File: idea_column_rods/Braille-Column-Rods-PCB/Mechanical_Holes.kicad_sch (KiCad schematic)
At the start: 14 parts

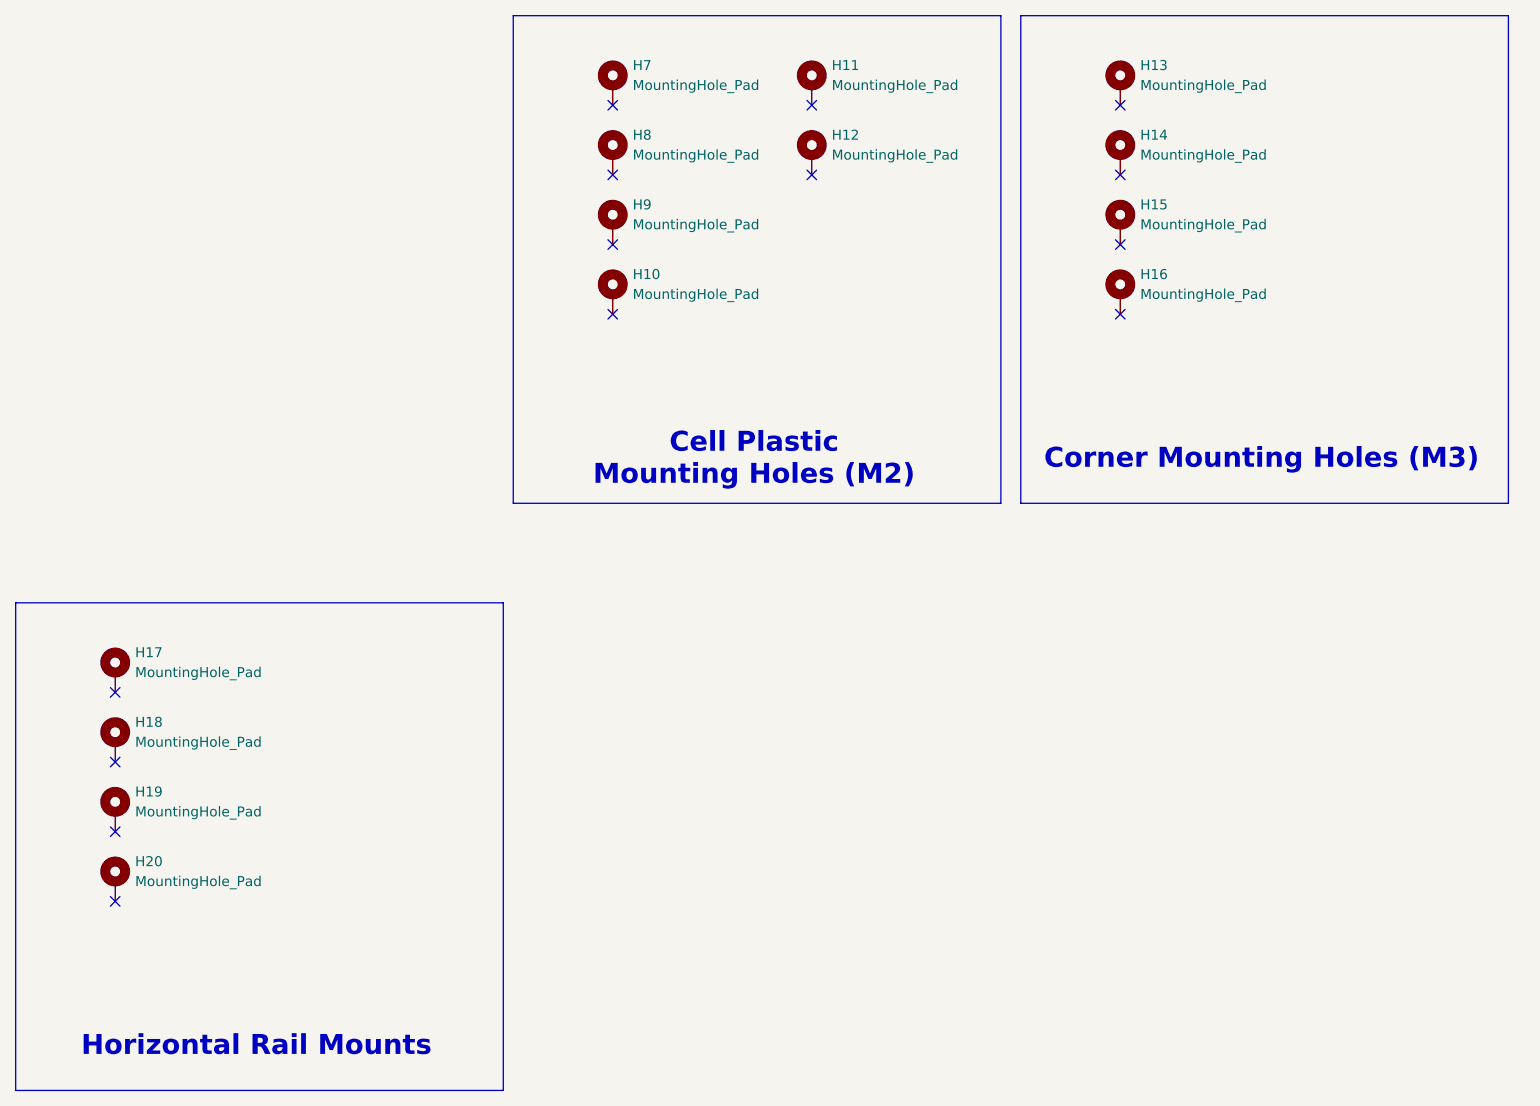
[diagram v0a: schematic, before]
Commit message: WIP: Rods PCB placement
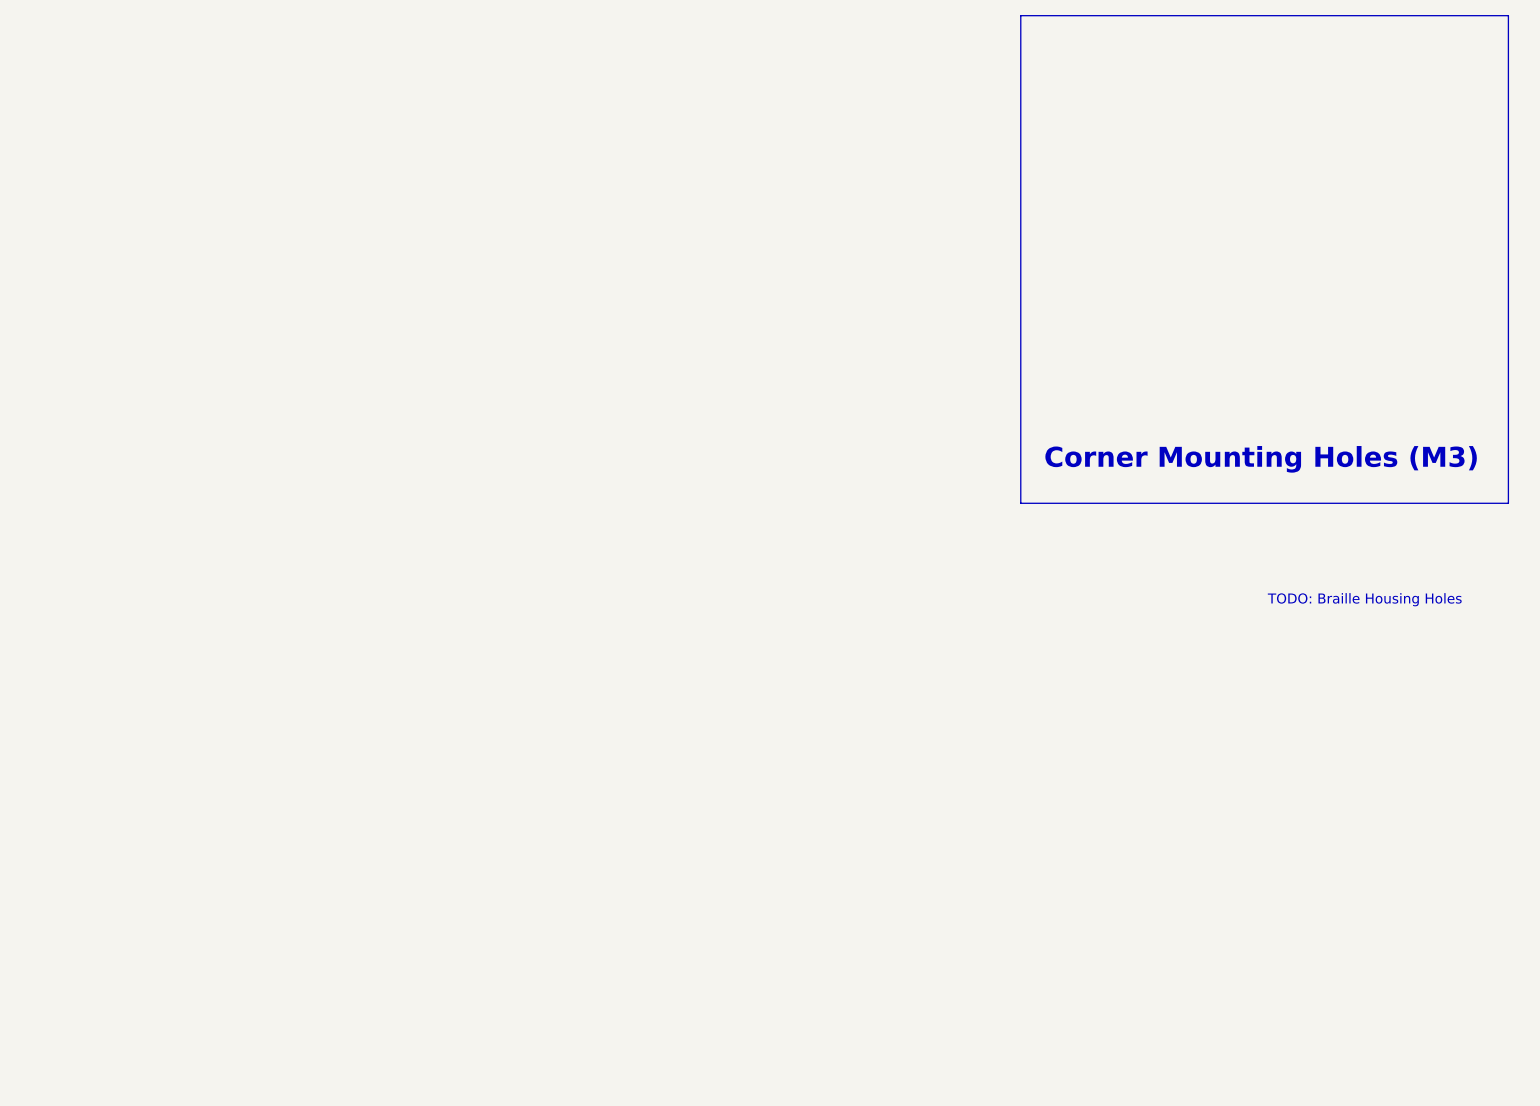
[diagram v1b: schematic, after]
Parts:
- removed H10, H11, H12, H7, H8, H9: MountingHole_Pad, 00-lib-footprints:MountingHole_2.2mm_M2_Pad_NoSilk, symbol Mechanical:MountingHole_Pad
- removed H13, H14, H15, H16: MountingHole_Pad, 00-lib-footprints:MountingHole_3.2mm_M3_Pad_NoSilk, symbol Mechanical:MountingHole_Pad
- removed H17, H18, H19, H20: MountingHole_Pad, 00-lib-footprints:HorizMounting_4x_M2_and_M3_Middle, symbol Mechanical:MountingHole_Pad
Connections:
- no-connect marks 14 -> 0
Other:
- note added: "TODO: Braille Housing Holes"
- note removed: "Cell Plastic Mounting Holes (M2)"
- note removed: "Horizontal Rail Mounts"

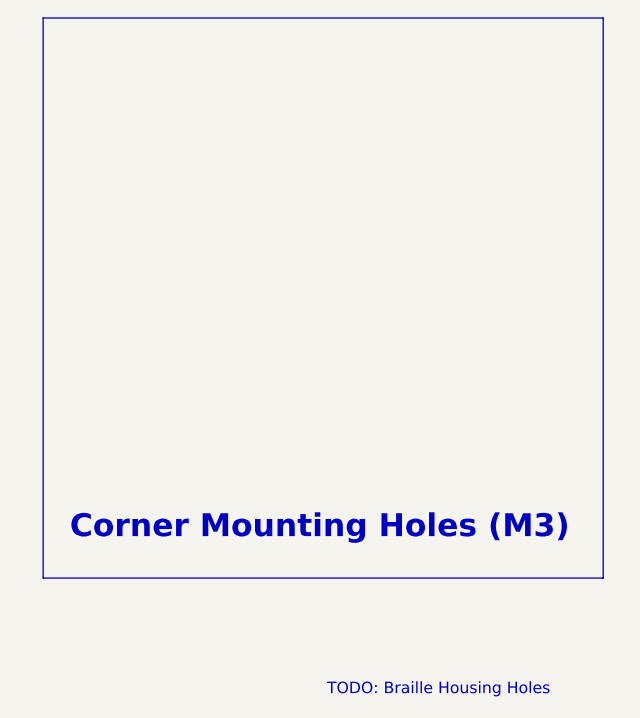
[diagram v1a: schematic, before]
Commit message: WIP: Place the housing and motor X
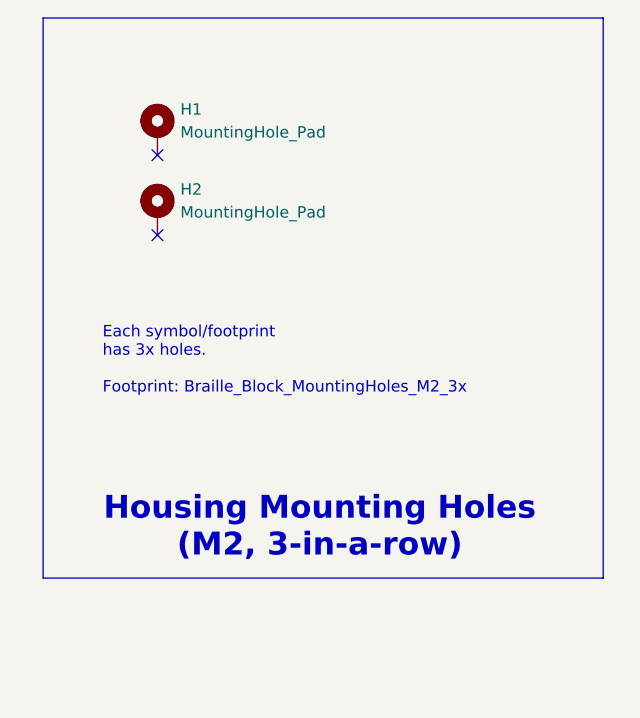
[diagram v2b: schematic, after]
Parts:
- added H1, H2: MountingHole_Pad, 00-lib-footprints:Braille_Block_MountingHoles_M2_3x, symbol Mechanical:MountingHole_Pad
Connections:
- no-connect marks 0 -> 2
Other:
- note added: "Each symbol/footprint has 3x holes. Footprint: Braille_Block_MountingHoles_M2_3x"
- note added: "Housing Mounting Holes (M2, 3-in-a-row)"
- note removed: "Corner Mounting Holes (M3)"
- note removed: "TODO: Braille Housing Holes"
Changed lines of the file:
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@@
 	(generator_version "8.0")
 	(paper "USLetter")
+	(no_connect
+		(at 168.91 50.8)
+	)
+	(no_connect
+		(at 168.91 41.91)
+	)
 	(rectangle
 		(start 156.21 26.67)
@@
 		)
 	)
-	(text "Corner Mounting Holes (M3)"
+	(text "Each symbol/footprint\nhas 3x holes.\n\nFootprint: Braille_Block_MountingHoles_M2_3x"
+		(exclude_from_sim no)
+		(at 162.814 64.77 0)
+		(effects
+			(font
+				(size 1.27 1.27)
+			)
+			(justify left)
+		)
+	)
+	(text "Housing Mounting Holes\n(M2, 3-in-a-row)"
 		(exclude_from_sim no)
 		(at 186.944 83.312 0)
@@
 		)
 	)
-	(text "TODO: Braille Housing Holes"
-		(exclude_from_sim no)
-		(at 200.152 101.346 0)
-		(effects
-			(font
-				(size 1.27 1.27)
+	(symbol
+		(lib_id "Mechanical:MountingHole_Pad")
+		(at 168.91 39.37 0)
+		(unit 1)
+		(exclude_from_sim yes)
+		(in_bom no)
+		(on_board yes)
+		(dnp no)
+		(fields_autoplaced yes)
+		(property "Reference" "H1"
+			(at 171.45 36.8299 0)
+			(effects
+				(font
+					(size 1.27 1.27)
+				)
+				(justify left)
 			)
 		)
+		(property "Value" "MountingHole_Pad"
+			(at 171.45 39.3699 0)
+			(effects
+				(font
+					(size 1.27 1.27)
+				)
+				(justify left)
+			)
+		)
+		(property "Footprint" "00-lib-footprints:Braille_Block_MountingHoles_M2_3x"
+			(at 168.91 39.37 0)
+			(effects
+				(font
+					(size 1.27 1.27)
+				)
+				(hide yes)
+			)
+		)
+		(property "Datasheet" "~"
+			(at 168.91 39.37 0)
+			(effects
+				(font
+					(size 1.27 1.27)
+				)
+				(hide yes)
+			)
+		)
+		(property "Description" "Mounting Hole with connection"
+			(at 168.91 39.37 0)
+			(effects
+				(font
+					(size 1.27 1.27)
+				)
+				(hide yes)
+			)
+		)
+		(pin "1"
+		)
+		(instances
+			(project ""
+				(path "/f7fdfeea-4cd4-4338-ad68-f9089a17ed6f/68ef9985-9a74-4d11-86d2-dc4810a2b95d"
+					(reference "H1")
+					(unit 1)
+				)
+			)
+		)
+	)
+	(symbol
+		(lib_id "Mechanical:MountingHole_Pad")
+		(at 168.91 48.26 0)
+		(unit 1)
+		(exclude_from_sim yes)
+		(in_bom no)
+		(on_board yes)
+		(dnp no)
+		(fields_autoplaced yes)
+		(property "Reference" "H2"
+			(at 171.45 45.7199 0)
+			(effects
+				(font
+					(size 1.27 1.27)
+				)
+				(justify left)
+			)
+		)
+		(property "Value" "MountingHole_Pad"
+			(at 171.45 48.2599 0)
+			(effects
+				(font
+					(size 1.27 1.27)
+				)
+				(justify left)
+			)
+		)
+		(property "Footprint" "00-lib-footprints:Braille_Block_MountingHoles_M2_3x"
+			(at 168.91 48.26 0)
+			(effects
+				(font
+					(size 1.27 1.27)
+				)
+				(hide yes)
+			)
+		)
+		(property "Datasheet" "~"
+			(at 168.91 48.26 0)
+			(effects
+				(font
+					(size 1.27 1.27)
+				)
+				(hide yes)
+			)
+		)
+		(property "Description" "Mounting Hole with connection"
+			(at 168.91 48.26 0)
+			(effects
+				(font
+					(size 1.27 1.27)
+				)
+				(hide yes)
+			)
+		)
+		(pin "1"
+		)
+		(instances
+			(project "Braille-Column-Rods-PCB"
+				(path "/f7fdfeea-4cd4-4338-ad68-f9089a17ed6f/68ef9985-9a74-4d11-86d2-dc4810a2b95d"
+					(reference "H2")
+					(unit 1)
+				)
+			)
+		)

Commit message: Complete type 4 rev 1
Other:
- title: (none) -> Braille Cam Rod Prototype (Type 4)
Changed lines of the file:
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@@
 	(generator_version "8.0")
 	(paper "USLetter")
+	(title_block
+		(title "Braille Cam Rod Prototype (Type 4)")
+		(date "2025-01-06")
+		(rev "Rev 1")
+	)
 	(no_connect
 		(at 168.91 50.8)
